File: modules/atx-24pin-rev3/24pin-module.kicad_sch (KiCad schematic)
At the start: 74 parts, among them J1 TO-HUB, J2 TO-HUB-PWR, J3 ATX-24 PSU, J5 USB-C 2.0, J6 TO-HUB-STACK, SW1 BOOT, SW2 RESET, U1 ESP32-C6-MINI-1-N4, U10 INA238, U11 INA238, U12 INA238, U13 INA238, U2 TJA1051T/3, U3 LP5907MFX-3.3, U5 TPS2121RUXR, U612V1 INA181A2IDBVR, U65V1 INA181A2IDBVR, U712V1 TLV7011DBVR, U75V1 TLV7011DBVR

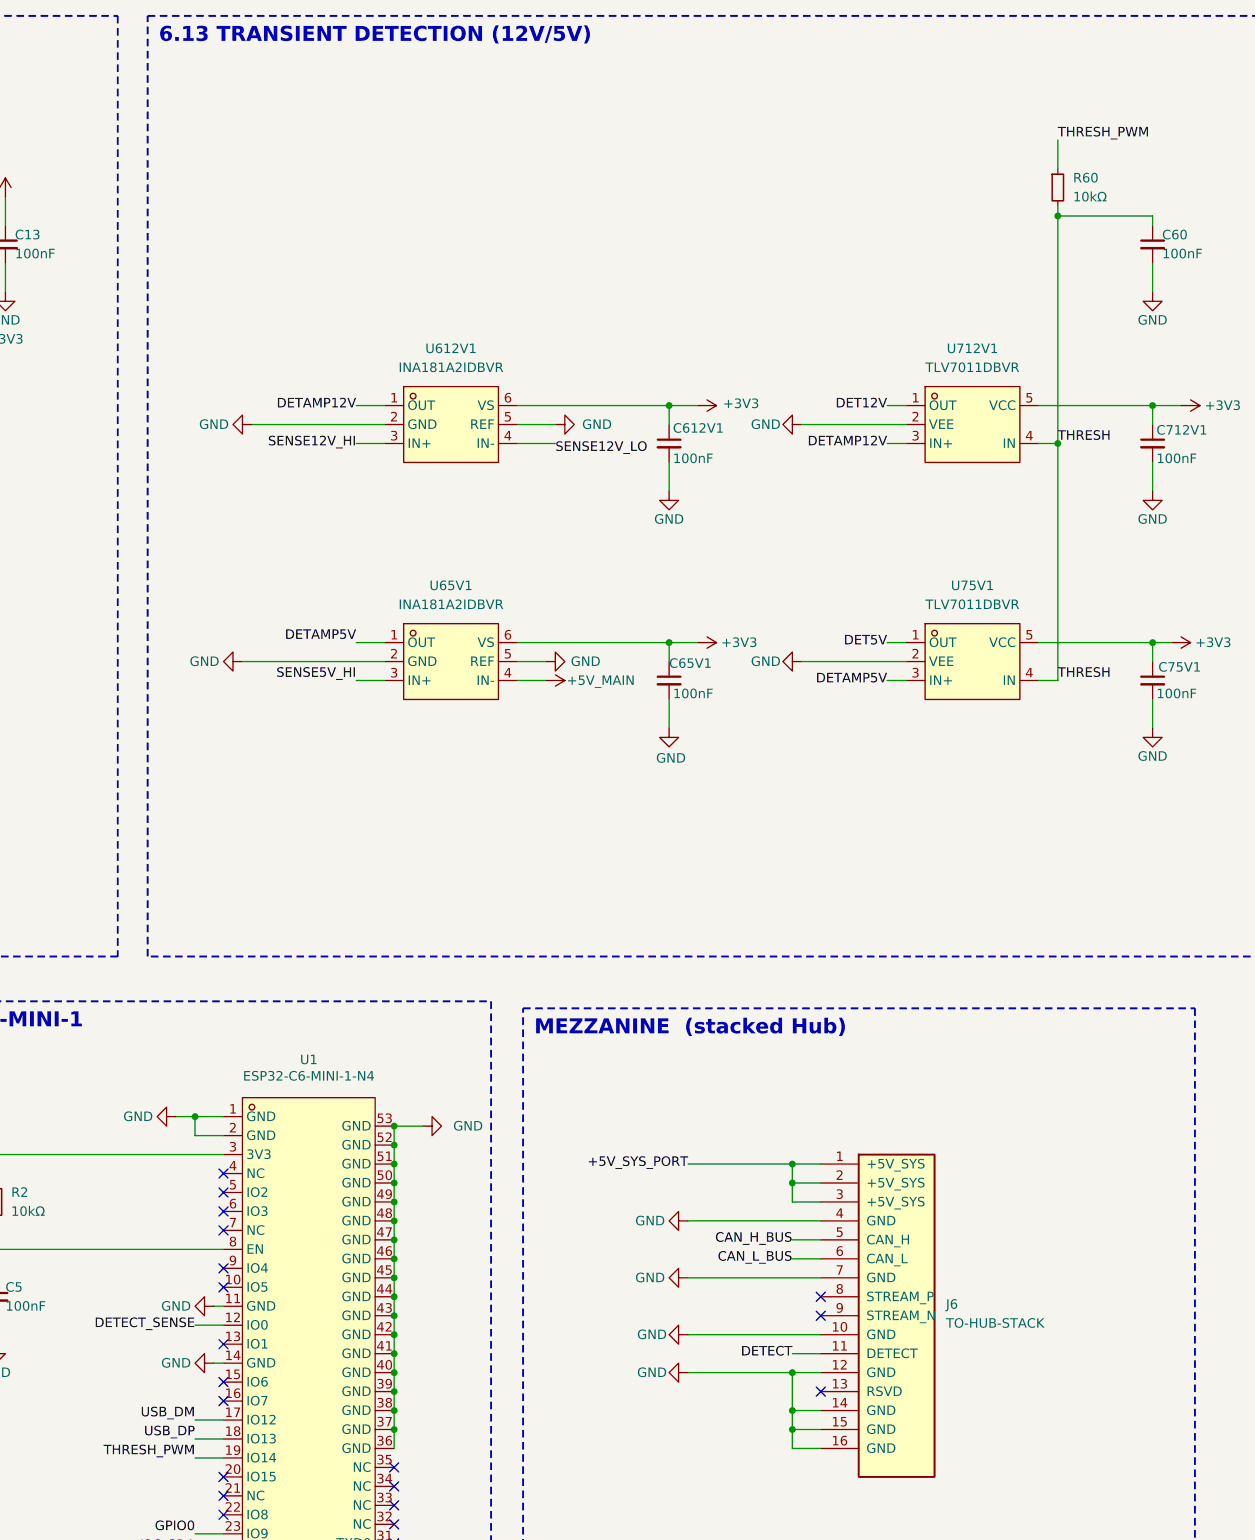
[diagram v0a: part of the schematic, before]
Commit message: 24-pin: add INA181+TLV7011 fast-detection cells on 3V3 + 5VSB rails
All four rails (12V/5V/3V3/5VSB) now carry the Sec 6.13-style fast-detection
front end, matching the existing 12V/5V cells (INA181A2 amp taps the rail's
shunt Kelvin pair -> TLV7011 comparator vs the board-shared /THRESH -> a free
MCU GPIO). Owner directive 2026-07-07: full total monitor.

New parts: U63V31/U73V31/C63V31 (3V3), U65VSB1/U75VSB1/C65VSB1 (5VSB).
DET3V3 -> C6 IO6 (pin15), DET5VSB -> C6 IO7 (pin16); the two stale no_connect
flags on those pins removed. Section caption updated to all four rails.

Netlist-verified: 0 unexpected changes vs HEAD (only the 4 new nets +
additive taps on SENSE3V3/5VSB_HI/LO, THRESH, +3V3, GND). ERC no_connect_connected
cleared; residual deltas are the documented-benign lib_symbol_mismatch /
Unspecified-pin classes (ERC skipped for DRAFT). Splice script committed.

Co-Authored-By: Claude Opus 4.8 <noreply@anthropic.com>
Claude-Session: https://claude.ai/code/session_01LvfqcnEeuin2oyJQw548EX
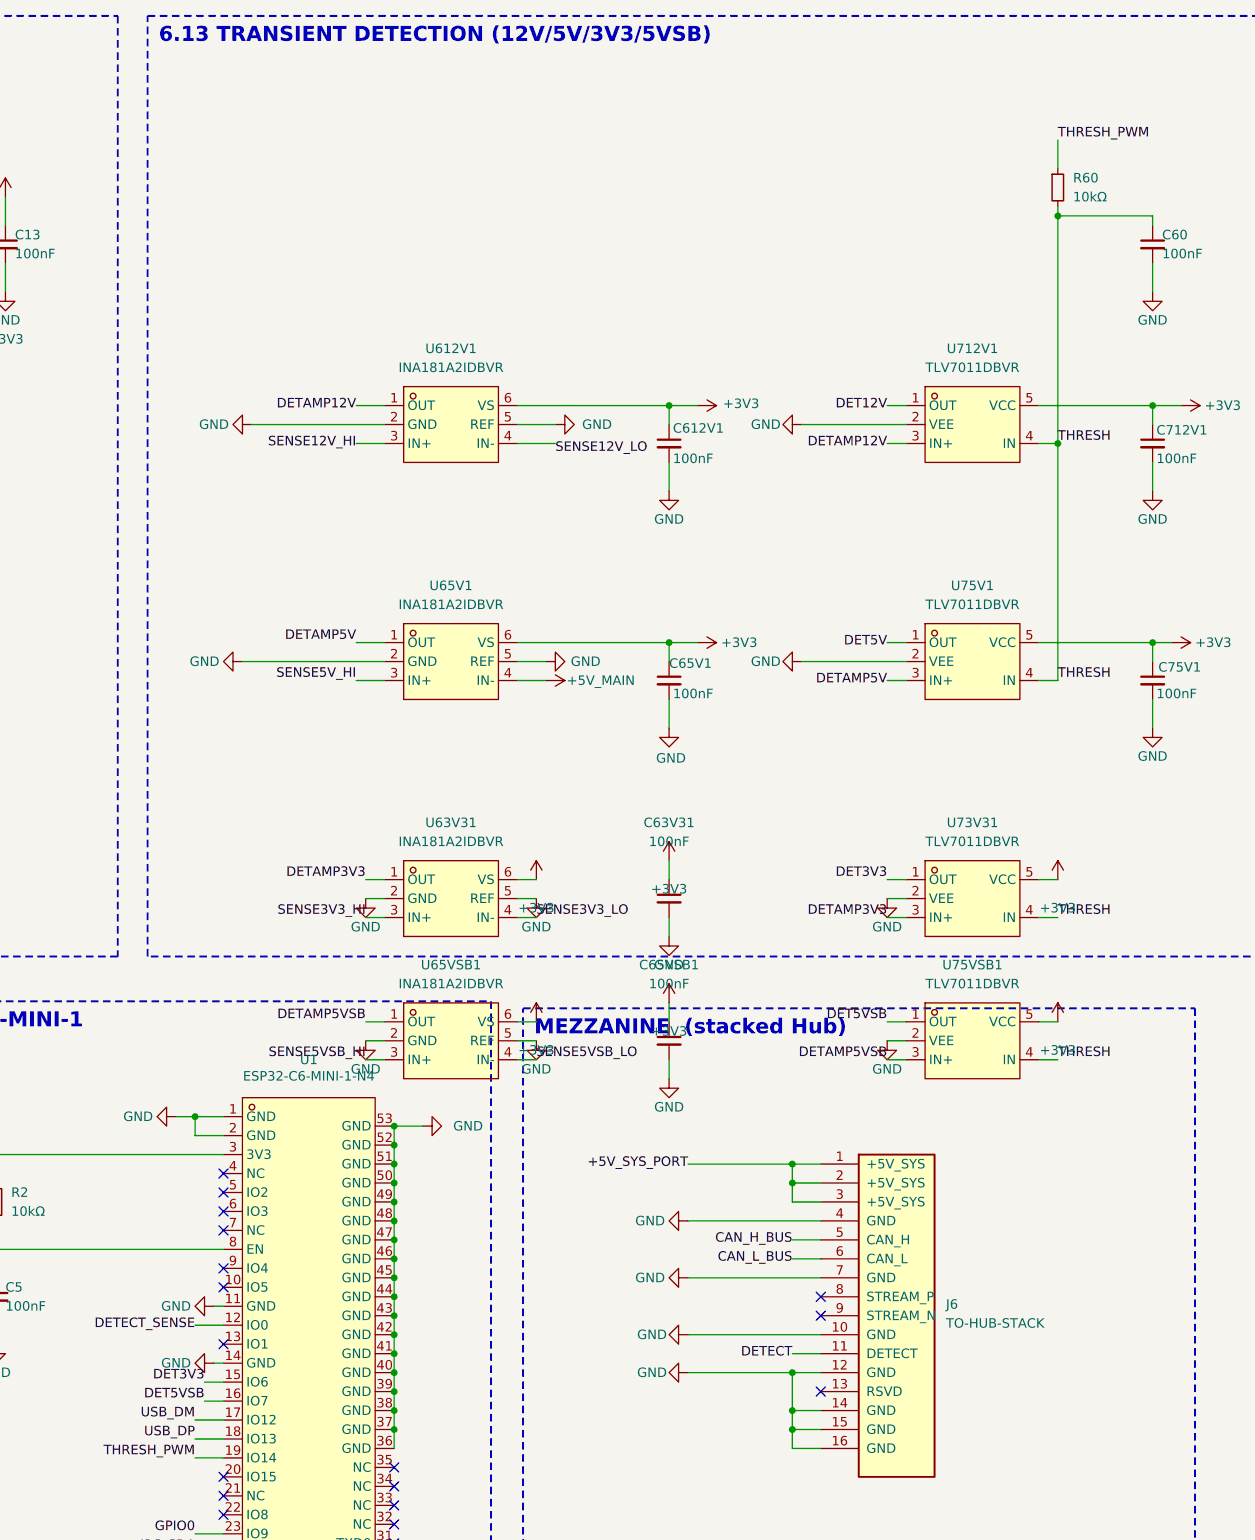
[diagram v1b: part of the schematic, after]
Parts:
- added C63V31, C65VSB1: 100nF, cec-Capacitor_SMD:C_0402_1005Metric, symbol cec-vendor:C_Small
- added U63V31, U65VSB1: INA181A2IDBVR, cec-Package_TO_SOT_SMD:SOT-23-6, symbol cec-vendor:INA181A2IDBVR
- added U73V31, U75VSB1: TLV7011DBVR, cec-Package_TO_SOT_SMD:SOT-23-5, symbol cec-vendor:TLV7011DBVR
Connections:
- net +3V3: now also C63V31.1, C65VSB1.1, U63V31.6 (VS), U65VSB1.6 (VS), U73V31.5 (VCC), U75VSB1.5 (VCC)
- net GND: now also C63V31.2, C65VSB1.2, U63V31.2 (GND), U63V31.5 (REF), U65VSB1.2 (GND), U65VSB1.5 (REF), U73V31.2 (VEE), U75VSB1.2 (VEE)
- net SENSE3V3_HI: now also U63V31.3 (IN+)
- net SENSE3V3_LO: now also U63V31.4 (IN-)
- net SENSE5VSB_HI: now also U65VSB1.3 (IN+)
- net SENSE5VSB_LO: now also U65VSB1.4 (IN-)
- net THRESH: now also U73V31.4 (IN), U75VSB1.4 (IN)
- net DET3V3: now reaches U1.15 (IO6)
- net DET3V3: now also U73V31.1 (OUT)
- net DET5VSB: now reaches U1.16 (IO7)
- net DET5VSB: now also U75VSB1.1 (OUT)
- new net DETAMP3V3: U63V31.1 (OUT), U73V31.3 (IN+)
- new net DETAMP5VSB: U65VSB1.1 (OUT), U75VSB1.3 (IN+)
- no-connect marks 39 -> 37
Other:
- note added: "6.13 TRANSIENT DETECTION (12V/5V/3V3/5VSB)"
- note removed: "6.13 TRANSIENT DETECTION (12V/5V)"

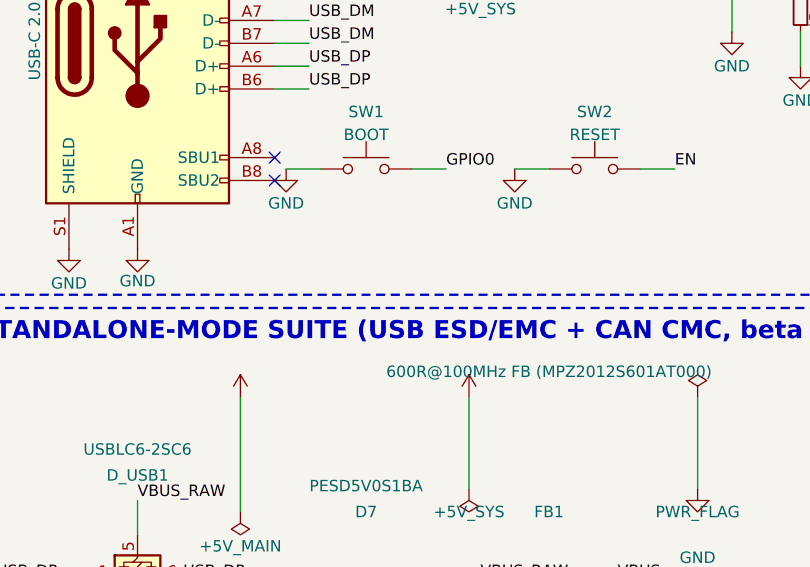
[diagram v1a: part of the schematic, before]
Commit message: All 5 sensing modules: add GPIO0 strapping-pin decoupler (match Hub)
Adds a 0.1uF cap (GPIO0->GND) + 10k pull-up (+3V3->GPIO0) to each module's
MCU sheet, matching the Hub (C8+R11). The modules already had BOOT+RESET
buttons and the EN reset RC; this closes the one systematic gap found in the
2026-07-07 decoupler audit -- the Espressif-recommended strapping-pin RC that
debounces the BOOT button and hardens GPIO0 against spurious download-mode
entry from noise. Owner directive 2026-07-07.

Parts: 24-pin C61/R61, eps/pcie-2/pcie-3 C41/R13, 12vhpwr C25/R24. Each lands
on /GPIO0 = {cap, pull-up, SW1(BOOT), MCU} with cap->GND and pull-up->+3V3,
netlist-verified 0 unexpected changes vs HEAD (an earlier placement that merged
GPIO0 with I2C_SCL/ISENSEP2 was caught by the diff and re-placed in
wire/label-clear space). ERC no_connect_connected=0 on all five.

Co-Authored-By: Claude Opus 4.8 <noreply@anthropic.com>
Claude-Session: https://claude.ai/code/session_01LvfqcnEeuin2oyJQw548EX
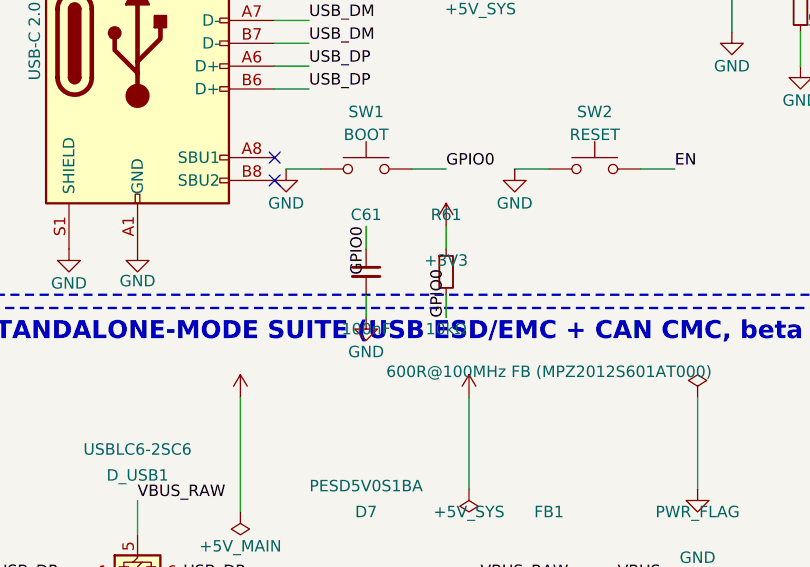
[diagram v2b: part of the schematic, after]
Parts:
- added C61: 100nF, cec-Capacitor_SMD:C_0402_1005Metric, symbol cec-vendor:C_Small
- added R61: 10kΩ, cec-Resistor_SMD:R_0402_1005Metric, symbol cec-vendor:R_Small
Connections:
- net +3V3: now also R61.1
- net GND: now also C61.2
- net GPIO0: now also C61.1, R61.2
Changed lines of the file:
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@@
 		(stroke (width 0) (type default)))
 	(label "DET5VSB" (at 261.62 209.55 180) (effects (font (size 1.27 1.27)) (justify right bottom)))
+	(symbol
+		(lib_id "cec-vendor:C_Small")
+		(at 69.85 300.99 0)
+		(unit 1)
+		(exclude_from_sim no)
+		(in_bom yes)
+		(on_board yes)
+		(dnp no)
+		(fields_autoplaced yes)
+		(property "Reference" "C61" (at 69.85 294.64 0) (effects (font (size 1.27 1.27))))
+		(property "Value" "100nF" (at 69.85 307.34 0) (effects (font (size 1.27 1.27))))
+		(property "Footprint" "cec-Capacitor_SMD:C_0402_1005Metric" (at 69.85 300.99 0) (effects (font (size 1.27 1.27)) (hide yes)))
+		(property "Datasheet" "" (at 69.85 300.99 0) (effects (font (size 1.27 1.27)) (hide yes)))
+		(pin "1")
+		(pin "2")
+		(instances
+			(project "24pin-module"
+				(path "/a4774022-41d4-4be7-85b6-fed5477a3f9f" (reference "C61") (unit 1))
+			)
+		)
+	)
+	(wire (pts (xy 69.85 298.45) (xy 69.85 295.91))
+		(stroke (width 0) (type default)))
+	(label "GPIO0" (at 69.85 295.91 90) (effects (font (size 1.27 1.27)) (justify right bottom)))
+	(wire (pts (xy 69.85 303.53) (xy 69.85 306.07))
+		(stroke (width 0) (type default)))
+	(symbol
+		(lib_id "cec-power:GND")
+		(at 69.85 306.07 0)
+		(unit 1)
+		(exclude_from_sim no)
+		(in_bom yes)
+		(on_board yes)
+		(dnp no)
+		(property "Reference" "#PWR0930" (at 69.85 303.53 0) (effects (font (size 1.27 1.27)) (hide yes)))
+		(property "Value" "GND" (at 69.85 309.88 0) (effects (font (size 1.27 1.27))))
+		(pin "1")
+		(instances
+			(project "24pin-module"
+				(path "/a4774022-41d4-4be7-85b6-fed5477a3f9f" (reference "#PWR0930") (unit 1))
+			)
+		)
+	)
+	(symbol
+		(lib_id "cec-vendor:R_Small")
+		(at 78.74 300.99 0)
+		(unit 1)
+		(exclude_from_sim no)
+		(in_bom yes)
+		(on_board yes)
+		(dnp no)
+		(fields_autoplaced yes)
+		(property "Reference" "R61" (at 78.74 294.64 0) (effects (font (size 1.27 1.27))))
+		(property "Value" "10kΩ" (at 78.74 307.34 0) (effects (font (size 1.27 1.27))))
+		(property "Footprint" "cec-Resistor_SMD:R_0402_1005Metric" (at 78.74 300.99 0) (effects (font (size 1.27 1.27)) (hide yes)))
+		(property "Datasheet" "" (at 78.74 300.99 0) (effects (font (size 1.27 1.27)) (hide yes)))
+		(pin "1")
+		(pin "2")
+		(instances
+			(project "24pin-module"
+				(path "/a4774022-41d4-4be7-85b6-fed5477a3f9f" (reference "R61") (unit 1))
+			)
+		)
+	)
+	(wire (pts (xy 78.74 298.45) (xy 78.74 295.91))
+		(stroke (width 0) (type default)))
+	(symbol
+		(lib_id "cec-power:+3V3")
+		(at 78.74 295.91 0)
+		(unit 1)
+		(exclude_from_sim no)
+		(in_bom yes)
+		(on_board yes)
+		(dnp no)
+		(property "Reference" "#PWR0931" (at 78.74 293.37 0) (effects (font (size 1.27 1.27)) (hide yes)))
+		(property "Value" "+3V3" (at 78.74 299.72 0) (effects (font (size 1.27 1.27))))
+		(pin "1")
+		(instances
+			(project "24pin-module"
+				(path "/a4774022-41d4-4be7-85b6-fed5477a3f9f" (reference "#PWR0931") (unit 1))
+			)
+		)
+	)
+	(wire (pts (xy 78.74 303.53) (xy 78.74 306.07))
+		(stroke (width 0) (type default)))
+	(label "GPIO0" (at 78.74 306.07 270) (effects (font (size 1.27 1.27)) (justify left bottom)))
 	(sheet_instances
 		(path "/"
